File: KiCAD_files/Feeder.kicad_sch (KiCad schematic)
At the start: 64 parts, among them J301 Conn_01x03, Q301 60V N channel, Q302 TK13P25D,RQ, T301 PA2467NL, U301 NCP12700, U302 HMHA2801A, U303 HMHA2801A, U304 TL431MFDT,215, U305 TL431MFDT,215

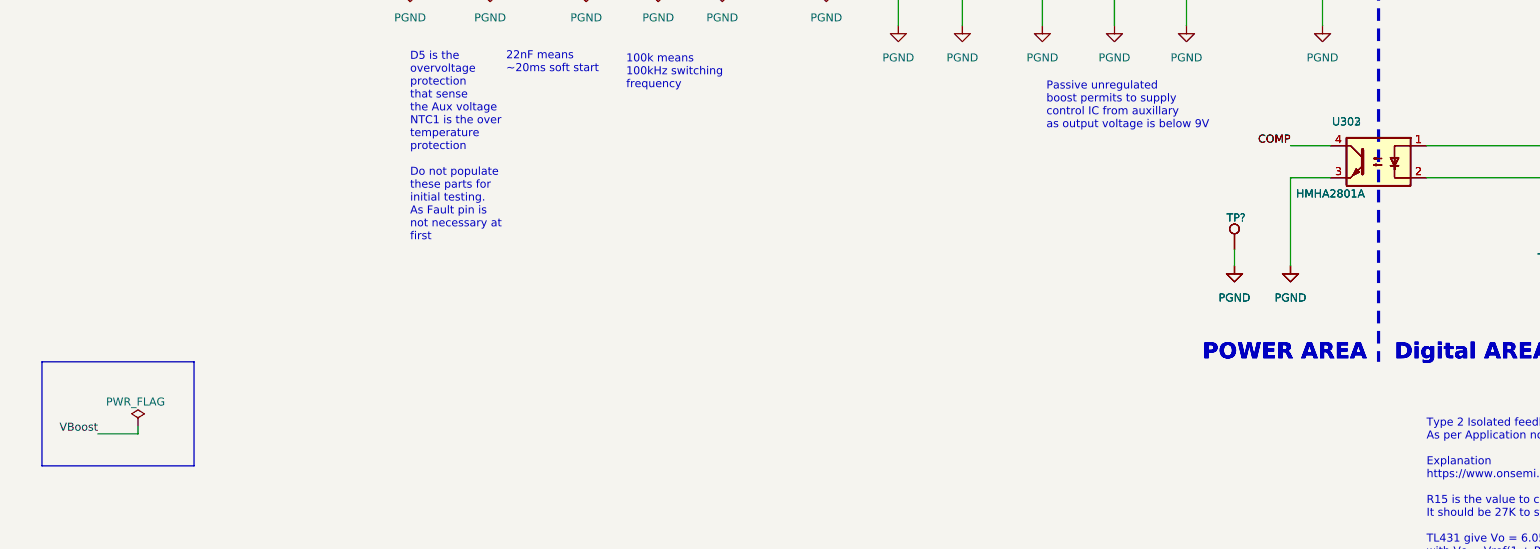
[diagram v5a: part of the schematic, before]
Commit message: full hierarchical sheet
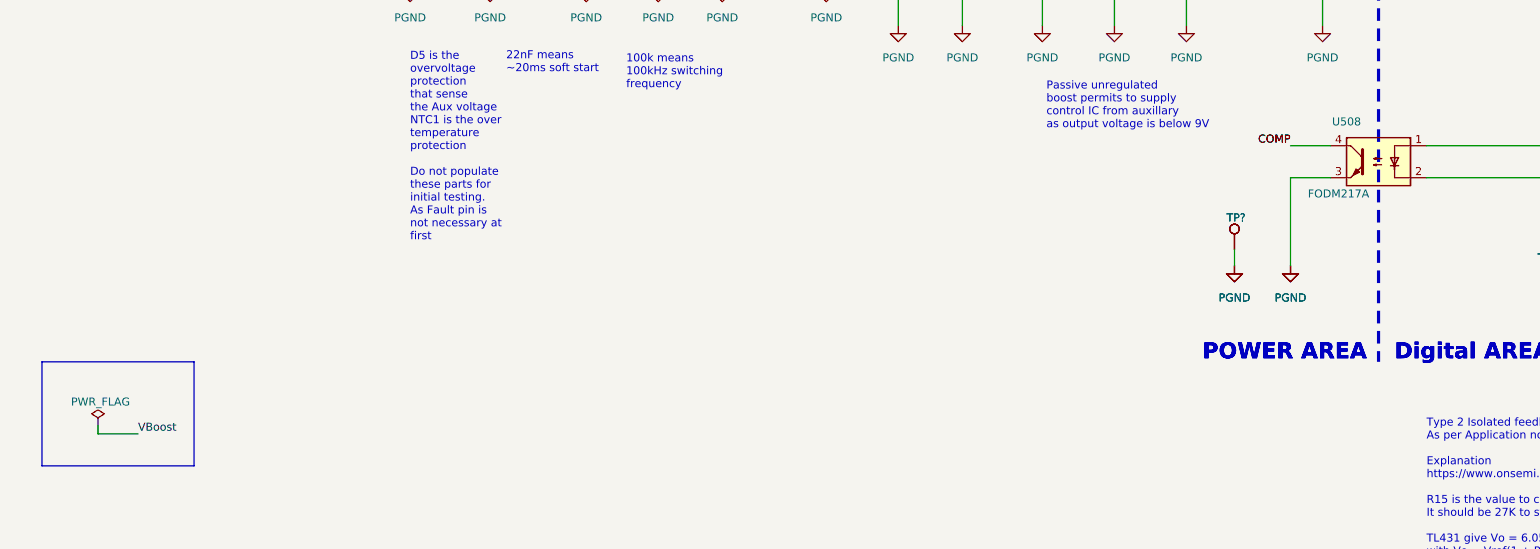
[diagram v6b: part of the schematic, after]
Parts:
- removed U302, U303: HMHA2801A, Package_DIP:SMDIP-4_W9.53mm_Clearance8mm, symbol Isolator:SFH617A-1X007T
- added U508: FODM217A, Package_DIP:SMDIP-4_W9.53mm_Clearance8mm, symbol Isolator:SFH617A-1X007T
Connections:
- net COMP: now also U508.4
- net GND: now also U508.3
- net at R314.2, R315.2, R316.1: now also U508.1
- net at C320.1, R316.2, U304.2 (K)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: now also U508.2
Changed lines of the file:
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@@
     (stroke (width 0) (type default))
   )
-  (wire (pts (xy 34.29 217.17) (xy 34.29 215.9))
+  (wire (pts (xy 27.94 217.17) (xy 27.94 215.9))
     (stroke (width 0) (type default))
   )
@@
     (stroke (width 0) (type default))
   )
-  (wire (pts (xy 27.94 217.17) (xy 34.29 217.17))
+  (wire (pts (xy 34.29 217.17) (xy 27.94 217.17))
     (stroke (width 0) (type default))
   )
@@
     (effects (font (size 1.27 1.27)) (justify left bottom))
   )
-  (label "VBoost" (at 27.94 217.17 180) (fields_autoplaced)
-    (effects (font (size 1.27 1.27)) (justify right bottom))
+  (label "VBoost" (at 34.29 217.17 0) (fields_autoplaced)
+    (effects (font (size 1.27 1.27)) (justify left bottom))
   )
   (label "VAUX" (at 100.33 80.01 180) (fields_autoplaced)
@@
     )
   )
-  (symbol (lib_id "Device:R") (at 154.94 143.51 0) (unit 1)
-    (in_bom yes) (on_board yes) (dnp no)
-    (property "Reference" "R304" (at 156.845 142.24 0)
-      (effects (font (size 1.27 1.27)) (justify left))
-    )
-    (property "Value" "1.4k" (at 156.845 144.78 0)
-      (effects (font (size 1.27 1.27)) (justify left))
-    )
-    (property "Footprint" "Footprints:R_0805_2012Metric" (at 153.162 143.51 90)
-      (effects (font (size 1.27 1.27)) hide)
-    )
-    (property "Datasheet" "~" (at 154.94 143.51 0)
-      (effects (font (size 1.27 1.27)) hide)
-    )
-    (property "manf#" "RC0805FR-071K4L" (at 154.94 143.51 0)
-      (effects (font (size 1.27 1.27)) hide)
-    )
-    (property "Package" "0805" (at 154.94 143.51 0)
-      (effects (font (size 1.27 1.27)) hide)
-    )
-    (pin "1")
-    (pin "2")
-    (instances
-      (project "inverter"
-        (path "/8d0c1d66-35ef-4a53-a28f-436a11b54f42/bce1534c-362e-45ed-a9dd-a44d6954485a"
-          (reference "R304") (unit 1)
-        )
-      )
-    )
-  )
-  (symbol (lib_id "power:GND") (at 177.8 152.4 0) (unit 1)
-    (in_bom yes) (on_board yes) (dnp no)
-    (property "Reference" "#PWR0314" (at 177.8 158.75 0)
-      (effects (font (size 1.27 1.27)) hide)
-    )
-    (property "Value" "PGND" (at 177.8 157.48 0)
-      (effects (font (size 1.27 1.27)))
-    )
-    (property "Footprint" "" (at 177.8 152.4 0)
-      (effects (font (size 1.27 1.27)) hide)
-    )
-    (property "Datasheet" "" (at 177.8 152.4 0)
-      (effects (font (size 1.27 1.27)) hide)
-    )
-    (pin "1")
-    (instances
-      (project "inverter"
-        (path "/8d0c1d66-35ef-4a53-a28f-436a11b54f42/bce1534c-362e-45ed-a9dd-a44d6954485a"
-          (reference "#PWR0314") (unit 1)
-        )
-      )
-    )
-  )
   (symbol (lib_id "Isolator:SFH617A-1X007T") (at 231.14 173.99 0) (mirror y) (unit 1)
     (in_bom yes) (on_board yes) (dnp no)
-    (property "Reference" "U302" (at 226.06 167.64 0)
-      (effects (font (size 1.27 1.27)))
-    )
-    (property "Value" "HMHA2801A " (at 223.52 179.07 0)
-      (effects (font (size 1.27 1.27)))
+    (property "Reference" "U508" (at 226.06 167.64 0)
+      (effects (font (size 1.27 1.27)))
+    )
+    (property "Value" "FODM217A" (at 223.52 179.07 0)
+      (effects (font (size 1.27 1.27)) hide)
     )
     (property "Footprint" "Package_DIP:SMDIP-4_W9.53mm_Clearance8mm" (at 231.14 182.88 0)
       (effects (font (size 1.27 1.27) italic) hide)
     )
-    (property "Datasheet" "http://www.vishay.com/docs/83740/sfh617a.pdf" (at 231.14 175.26 0)
+    (property "Datasheet" "https://www.onsemi.com/download/data-sheet/pdf/fodm214-d.pdf" (at 231.14 175.26 0)
       (effects (font (size 1.27 1.27)) (justify left) hide)
     )
-    (property "manf#" "FODM217A" (at 231.14 173.99 0)
-      (effects (font (size 1.27 1.27)) hide)
+    (property "manf#" "FODM217A" (at 224.79 179.07 0)
+      (effects (font (size 1.27 1.27)))
     )
     (pin "1")
@@
       (project "inverter"
         (path "/8d0c1d66-35ef-4a53-a28f-436a11b54f42/bce1534c-362e-45ed-a9dd-a44d6954485a"
-          (reference "U302") (unit 1)
+          (reference "U508") (unit 1)
+        )
+      )
+    )
+  )
+  (symbol (lib_id "Device:R") (at 154.94 143.51 0) (unit 1)
+    (in_bom yes) (on_board yes) (dnp no)
+    (property "Reference" "R304" (at 156.845 142.24 0)
+      (effects (font (size 1.27 1.27)) (justify left))
+    )
+    (property "Value" "1.4k" (at 156.845 144.78 0)
+      (effects (font (size 1.27 1.27)) (justify left))
+    )
+    (property "Footprint" "Footprints:R_0805_2012Metric" (at 153.162 143.51 90)
+      (effects (font (size 1.27 1.27)) hide)
+    )
+    (property "Datasheet" "~" (at 154.94 143.51 0)
+      (effects (font (size 1.27 1.27)) hide)
+    )
+    (property "manf#" "RC0805FR-071K4L" (at 154.94 143.51 0)
+      (effects (font (size 1.27 1.27)) hide)
+    )
+    (property "Package" "0805" (at 154.94 143.51 0)
+      (effects (font (size 1.27 1.27)) hide)
+    )
+    (pin "1")
+    (pin "2")
+    (instances
+      (project "inverter"
+        (path "/8d0c1d66-35ef-4a53-a28f-436a11b54f42/bce1534c-362e-45ed-a9dd-a44d6954485a"
+          (reference "R304") (unit 1)
+        )
+      )
+    )
+  )
+  (symbol (lib_id "power:GND") (at 177.8 152.4 0) (unit 1)
+    (in_bom yes) (on_board yes) (dnp no)
+    (property "Reference" "#PWR0314" (at 177.8 158.75 0)
+      (effects (font (size 1.27 1.27)) hide)
+    )
+    (property "Value" "PGND" (at 177.8 157.48 0)
+      (effects (font (size 1.27 1.27)))
+    )
+    (property "Footprint" "" (at 177.8 152.4 0)
+      (effects (font (size 1.27 1.27)) hide)
+    )
+    (property "Datasheet" "" (at 177.8 152.4 0)
+      (effects (font (size 1.27 1.27)) hide)
+    )
+    (pin "1")
+    (instances
+      (project "inverter"
+        (path "/8d0c1d66-35ef-4a53-a28f-436a11b54f42/bce1534c-362e-45ed-a9dd-a44d6954485a"
+          (reference "#PWR0314") (unit 1)
         )
       )
@@
         (path "/8d0c1d66-35ef-4a53-a28f-436a11b54f42/bce1534c-362e-45ed-a9dd-a44d6954485a"
           (reference "C301") (unit 1)
-        )
-      )
-    )
-  )
-  (symbol (lib_id "Isolator:SFH617A-1X007T") (at 231.14 173.99 0) (mirror y) (unit 1)
-    (in_bom yes) (on_board yes) (dnp no)
-    (property "Reference" "U303" (at 226.06 167.64 0)
-      (effects (font (size 1.27 1.27)))
-    )
-    (property "Value" "HMHA2801A " (at 223.52 179.07 0)
-      (effects (font (size 1.27 1.27)))
-    )
-    (property "Footprint" "Package_DIP:SMDIP-4_W9.53mm_Clearance8mm" (at 231.14 182.88 0)
-      (effects (font (size 1.27 1.27) italic) hide)
-    )
-    (property "Datasheet" "http://www.vishay.com/docs/83740/sfh617a.pdf" (at 231.14 175.26 0)
-      (effects (font (size 1.27 1.27)) (justify left) hide)
-    )
-    (property "manf#" "FODM217A" (at 231.14 173.99 0)
-      (effects (font (size 1.27 1.27)) hide)
-    )
-    (pin "1")
-    (pin "2")
-    (pin "3")
-    (pin "4")
-    (instances
-      (project "inverter"
-        (path "/8d0c1d66-35ef-4a53-a28f-436a11b54f42/bce1534c-362e-45ed-a9dd-a44d6954485a"
-          (reference "U303") (unit 1)
         )
       )
@@
     )
   )
-  (symbol (lib_id "power:PWR_FLAG") (at 34.29 215.9 0) (unit 1)
-    (in_bom yes) (on_board yes) (dnp no)
-    (property "Reference" "#FLG0101" (at 34.29 213.995 0)
-      (effects (font (size 1.27 1.27)) hide)
-    )
-    (property "Value" "PWR_FLAG" (at 29.21 212.09 0)
-      (effects (font (size 1.27 1.27)) (justify left))
-    )
-    (property "Footprint" "" (at 34.29 215.9 0)
-      (effects (font (size 1.27 1.27)) hide)
-    )
-    (property "Datasheet" "~" (at 34.29 215.9 0)
-      (effects (font (size 1.27 1.27)) hide)
-    )
+  (symbol (lib_id "power:PWR_FLAG") (at 27.94 215.9 0) (mirror y) (unit 1)
+    (in_bom yes) (on_board yes) (dnp no)
+    (property "Reference" "#FLG0101" (at 27.94 213.995 0)
+      (effects (font (size 1.27 1.27)) hide)
+    )
+    (property "Value" "PWR_FLAG" (at 33.02 212.09 0)
+      (effects (font (size 1.27 1.27)) (justify left))
+    )
+    (property "Footprint" "" (at 27.94 215.9 0)
+      (effects (font (size 1.27 1.27)) hide)
+    )
+    (property "Datasheet" "~" (at 27.94 215.9 0)
+      (effects (font (size 1.27 1.27)) hide)
+    )

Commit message: save before starting routing
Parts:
- removed GND301, GND302, VOUT_GND301, VOUT_GND302: TP?, TestPoint:TestPoint_THTPad_D2.0mm_Drill1.0mm, symbol Connector:TestPoint
- removed R315: 1.4k, Footprints:R_0805_2012Metric, symbol Device:R
- removed U305: TL431MFDT,215, Footprints:SOT-23_copy, symbol Reference_Voltage:TL431DBZ
- added TP? (x2): TestPoint, Footprints:TestPoint_THTPad_D1.5mm_Drill0.7mm, symbol Connector:TestPoint
- U503: renamed from U304; footprint Footprints:SOT-23_copy -> Package_TO_SOT_SMD:SOT-23
- renumbered C301 to C501, C302 to C502, C303 to C503, C304 to C504, C305 to C505, C306 to C506, C307 to C507, C308 to C508, C309 to C509, C310 to C510, C311 to C511, C312 to C512, C313 to C513, C314 to C514, C315 to C515, C316 to C516, C317 to C517, C318 to C518, C319 to C519, C320 to C520, C321 to C521, D301 to D501, D302 to D502, D303 to D503, D304 to D504, D305 to D505, D306 to D506, D307 to D507, J301 to J501, JP301 to JP501, L301 to L501, L302 to L502, NTC301 to NTC501, Q301 to Q501, Q302 to Q502, R301 to R501, R302 to R502, R303 to R503, R304 to R504, R305 to R505, R306 to R506, R307 to R507, R308 to R508, R309 to R509, R310 to R510, R311 to R511, R312 to R512, R313 to R513, R314 to R514, R316 to R515, R317 to R516, R318 to R517, R319 to R518, T301 to T501, U301 to U501, U508 to U502
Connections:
- net DGND: now also TP?.1
- net GND: now also TP?.1
- net at C520.2, R517.2, R518.1: now also U503.2 (REF); no longer U503.1 (REF)
- net at C520.1, R515.2, U502.2: now also U503.1 (K); no longer U503.2 (K)
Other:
- title: Inverter V0.1 -> OWNVERTER V0.1
- moved on the sheet: C512, C513, D502, D505, D506, L502, Q501, R504, R511, R512

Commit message: real before importing netlist
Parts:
- renumbered C501 to C139, C502 to C140, C503 to C141, C504 to C142, C505 to C143, C506 to C144, C507 to C145, C508 to C146, C509 to C147, C510 to C148, C511 to C149, C512 to C150, C513 to C151, C514 to C152, C515 to C153, C516 to C154, C517 to C155, C518 to C156, C519 to C157, C520 to C158, C521 to C159, D501 to D104, D502 to D105, D503 to D106, D504 to D107, D505 to D108, D506 to D109, D507 to D110, J501 to J113, JP501 to JP113, L501 to L102, L502 to L103, NTC501 to NTC101, Q501 to Q101, Q502 to Q102, R501 to R145, R502 to R146, R503 to R147, R504 to R148, R505 to R149, R506 to R150, R507 to R151, R508 to R152, R509 to R153, R510 to R154, R511 to R155, R512 to R156, R513 to R157, R514 to R158, R515 to R159, R516 to R160, R517 to R161, R518 to R162, T501 to T101, U501 to U114, U502 to U115, U503 to U116
